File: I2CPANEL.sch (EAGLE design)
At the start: 26 parts, among them IC1 MCP23017SO, IC2 128X64 OLED, J1 M10-SOCKET, J2 OLED

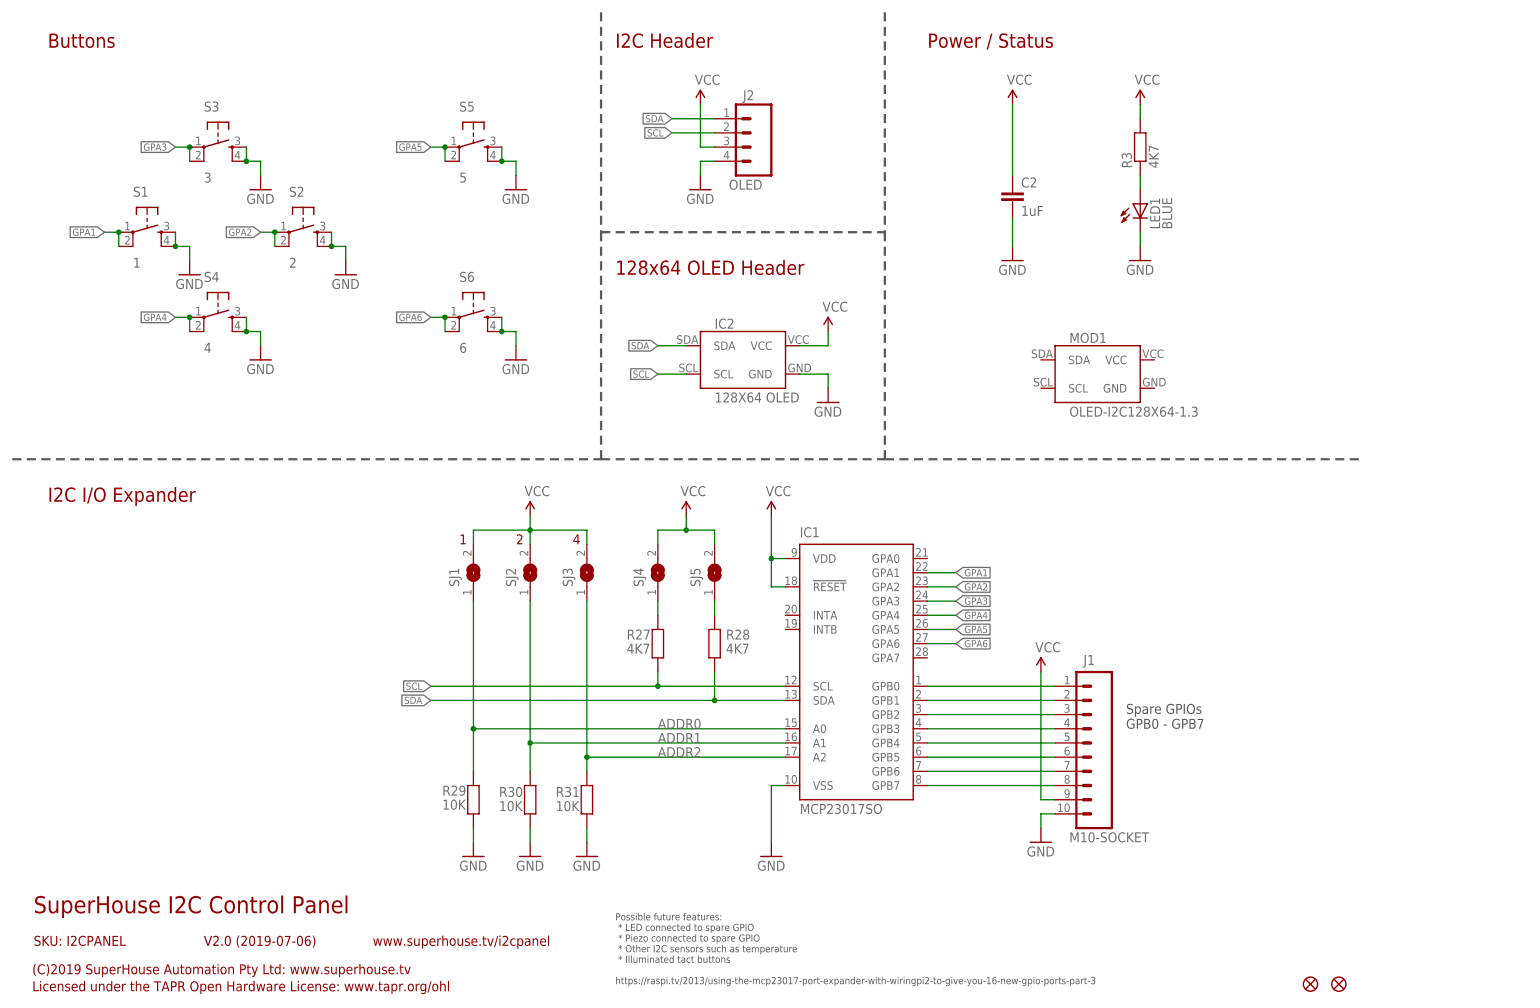
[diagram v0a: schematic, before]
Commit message: Renumbered designators to simplify BOM
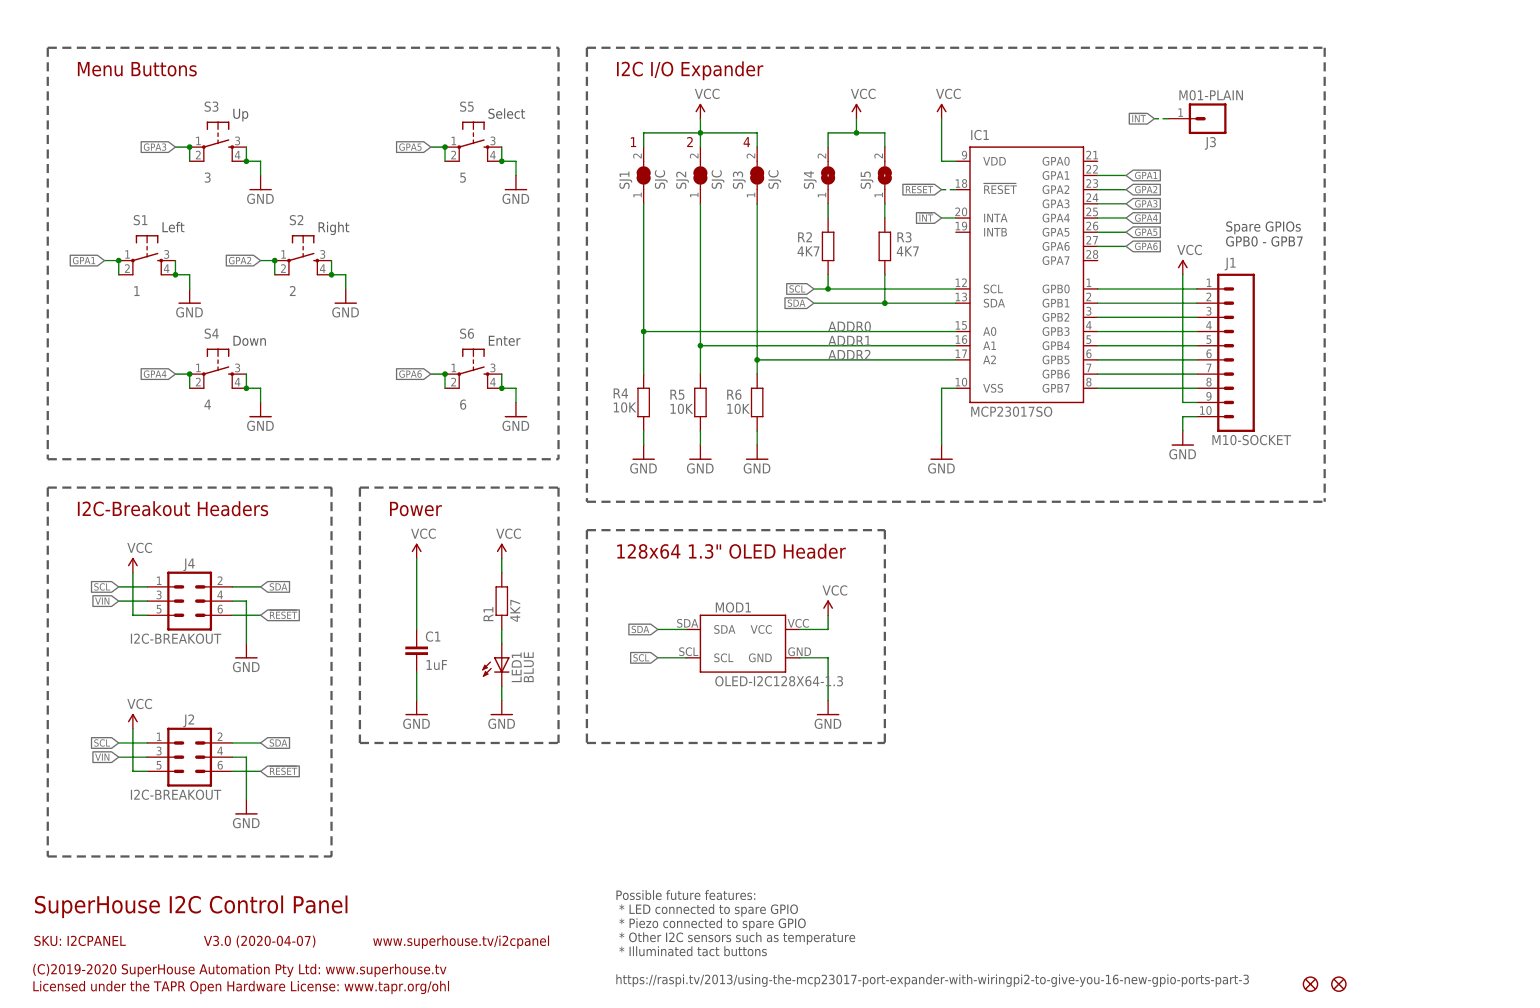
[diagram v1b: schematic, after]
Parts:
- removed C2: 1uF, SuperHouse-DiscreteSemi:CAP0603
- removed IC2: 128X64 OLED, freetronics-jon:OLED-I2C128X32
- removed R27, R28: 4K7, SuperHouse-DiscreteSemi:RESISTOR0603
- removed R29, R30, R31: 10K, SuperHouse-DiscreteSemi:RESISTOR0603
- added C1: 1uF, SuperHouse-DiscreteSemi:CAP0603
- added J3: M01-PLAIN, SuperHouse-Connectors:M01-PLAIN
- added J4: I2C-BREAKOUT, SuperHouse-Connectors:M02X3-SHROUDED
- added R1, R2: 4K7, SuperHouse-DiscreteSemi:RESISTOR0603
- added R4, R5, R6: 10K, SuperHouse-DiscreteSemi:RESISTOR0603
- J2: value OLED -> I2C-BREAKOUT; device SuperHouse-Connectors:M04-PIN -> SuperHouse-Connectors:M02X3-SHROUDED
- SJ1, SJ2, SJ3: value (none) -> SJC; device freetronics-jon:SJN -> SuperHouse-Jumpers:SJC-NORMAL
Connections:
- new net !INT: IC1.INTA, J3.1
- new net !RESET: IC1.!RESET, J2.6, J4.6
- new net VIN: J2.3, J4.3
- net ADDR0: now also R4.2; no longer R29.2
- net ADDR1: now also R5.2; no longer R30.2
- net ADDR2: now also R6.2; no longer R31.2
- net GND: now also C1.2, J4.4, MOD1.GND, R4.1, R5.1, R6.1; no longer C2.2, IC2.GND, R29.1, R30.1, R31.1
- net N$42: now also R2.2; no longer R27.2
- net N$43: now also R3.2; no longer R28.2
- net N$6: now also R1.1; no longer R3.1
- net SCL: now also J2.1, J4.1, MOD1.SCL, R2.1; no longer IC2.SCL, J2.2, R27.1
- net SDA: now also J2.2, J4.2, MOD1.SDA, R3.1; no longer IC2.SDA, J2.1, R28.1
- net VCC: now also C1.1, J2.5, J4.5, MOD1.VCC, R1.2; no longer C2.1, IC1.!RESET, IC2.VCC, J2.3, R3.2
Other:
- note added: "(C)2019-2020 SuperHouse Automation Pty Ltd: www.superhouse.tv"
- note added: "128x64 1.3" OLED Header"
- note added: "Down"
- note added: "Enter"
- note added: "I2C-Breakout Headers"
- note added: "Left"
- note added: "Menu Buttons"
- note added: "Power"
- note added: "Right"
- note added: "Select"
- note added: "Up"
- note added: "V3.0 (2020-04-07)"
- note removed: "(C)2019 SuperHouse Automation Pty Ltd: www.superhouse.tv"
- note removed: "128x64 OLED Header"
- note removed: "Buttons"
- note removed: "I2C Header"
- note removed: "Power / Status"
- note removed: "V2.0 (2019-07-06)"
- moved on the sheet: IC1, J1, LED1, MOD1, R3, S1, S2, S4, S6, SJ4, SJ5
